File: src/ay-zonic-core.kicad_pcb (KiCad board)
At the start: 2 copper layers, 63.5 x 80.1 mm, 31 parts, among them SW1 ZON-X, U1 AY-3-8912, U2 74HCT74, U3 74HCT08, U4 74HCT11, U5 74HCT02

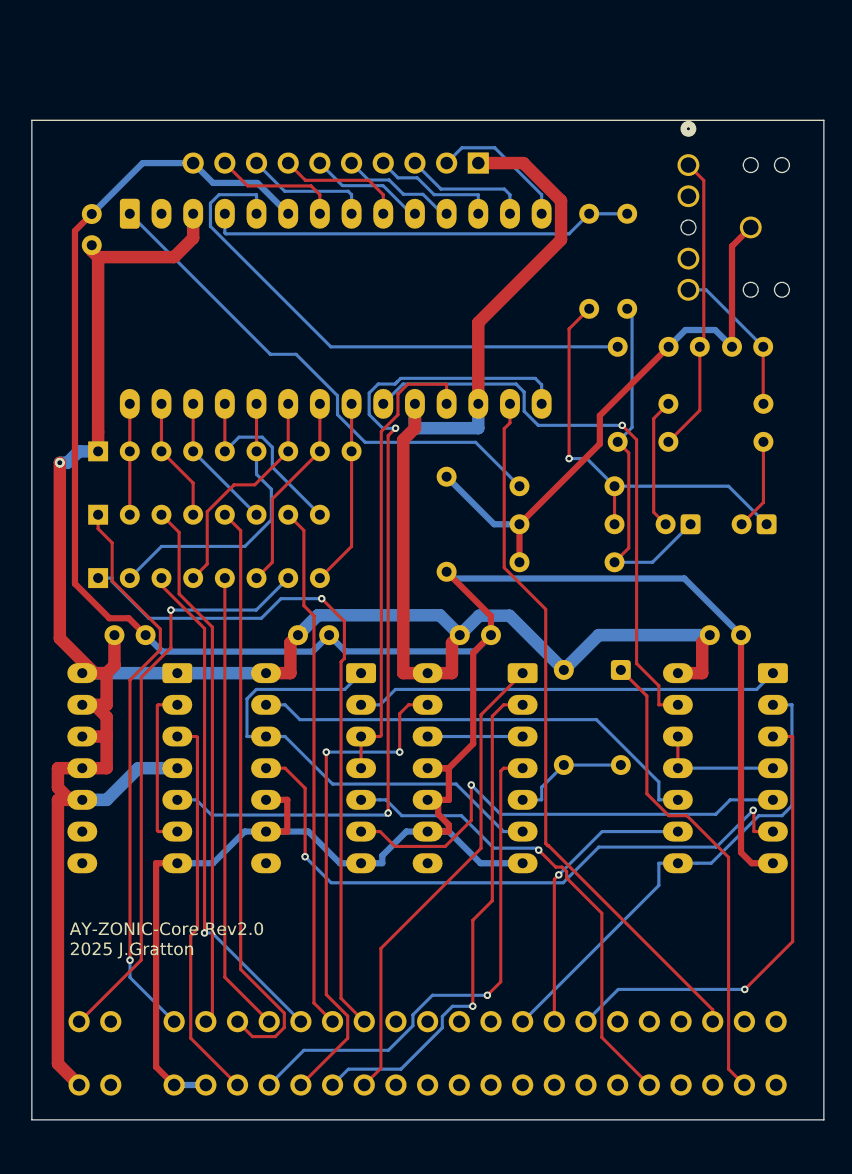
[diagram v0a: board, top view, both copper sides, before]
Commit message: added mounting holes and started routing.
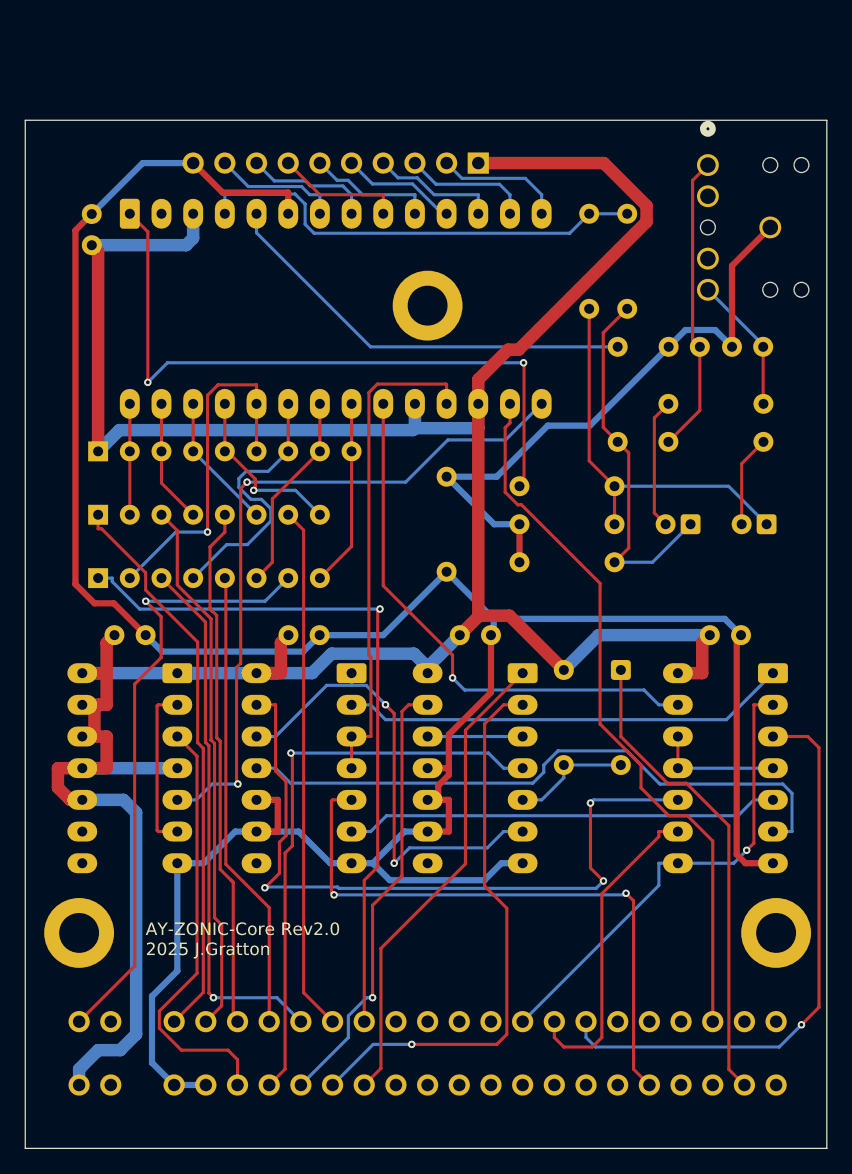
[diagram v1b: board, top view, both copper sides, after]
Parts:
- added H1: MountingHole, MountingHole:MountingHole_3.2mm_M3_DIN965_Pad, F.Cu at (123.2, 113.8)
- added H2: MountingHole, MountingHole:MountingHole_3.2mm_M3_DIN965_Pad, F.Cu at (67.3, 113.8)
- added H3: MountingHole, MountingHole:MountingHole_3.2mm_M3_DIN965_Pad, F.Cu at (95.2, 63.5)
- SW1: value ZON-X -> ZON X
- moved Line Out 1.56 mm to (117.7, 52.2)
- moved C7 0.76 mm to (84.1, 89.9)
- moved U3 0.76 mm to (89.2, 93.0)
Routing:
- net /IORD: track 37.0 -> 58.5 mm, vias 0 -> 3
- net /OUTC: track 41.2 -> 55.0 mm, vias 0 -> 2
- net /PSGCLK: track 69.2 -> 56.2 mm
- net VCC: track 234.9 -> 246.2 mm, vias 1 -> 0
- net /A7: track 38.7 -> 48.9 mm, vias 1 -> 2
- net /OUTA: track 44.0 -> 34.3 mm
- net /~{WR}: track 37.2 -> 46.5 mm
- net Net-(RN1-R5): track 23.1 -> 28.3 mm, vias 0 -> 1
- net /A0: track 41.3 -> 46.5 mm
- net /D2: track 47.6 -> 42.6 mm
- net GND: track 224.3 -> 219.7 mm
- net /A1: track 40.5 -> 35.9 mm, vias 2 -> 1
- net /BC1: track 47.2 -> 43.2 mm
- net /A2: track 41.1 -> 45.0 mm
- net Net-(U3-Pad6): track 38.7 -> 34.8 mm, vias 1 -> 0
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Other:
- board size 63.5 x 80.1 mm -> 64.3 x 82.4 mm

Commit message: updated routing
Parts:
- moved R4 1.52 mm to (112.8, 63.8)
- moved R5 1.52 mm to (109.7, 63.8)
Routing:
- net VCC: track 246.2 -> 220.6 mm
- net GND: track 219.7 -> 212.8 mm
- net /OUTA: track 34.3 -> 38.9 mm
- net /OUTC: track 55.0 -> 52.2 mm, vias 2 -> 1
- net /OUTB: track 36.7 -> 39.2 mm
- net Net-(RN1-R6): track 21.8 -> 23.9 mm
- net /IORD: track 58.5 -> 56.9 mm
- net Net-(RN1-R5): track 28.3 -> 29.9 mm
- net Net-(C2-Pad1): track 29.8 -> 31.0 mm
- net /~{IOREQ}: track 38.1 -> 36.9 mm
- net /LEFT: track 11.0 -> 12.1 mm
- net Net-(U2A-D): track 13.3 -> 12.4 mm
- net GND_AUDIO: track 49.6 -> 50.5 mm
- net /~{RESET}: track 57.6 -> 58.4 mm
- net Net-(C1-Pad1): track 31.6 -> 32.2 mm
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
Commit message: final route rev 2.0
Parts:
- added H4: MountingHole, MountingHole:MountingHole_3.2mm_M3_DIN965_Pad, F.Cu at (123.2, 45.7)
- SW1: value ZON X -> ZON-X
- moved H3 33.3 mm to (67.1, 45.7)
- moved I/O 5.59 mm to (99.3, 46.5)
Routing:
- net GND: track 212.8 -> 219.8 mm
- net /A2: track 45.0 -> 49.0 mm, vias 1 -> 0
- net /IOA5: track 9.90 -> 13.8 mm
- net /IOA3: track 9.30 -> 12.8 mm
- net /IOA7: track 9.72 -> 12.8 mm
- net /IOA4: track 9.75 -> 12.8 mm
- net /IOA2: track 10.2 -> 12.8 mm
- net /IOA6: track 10.2 -> 12.8 mm
- net /IOA0: track 10.2 -> 12.8 mm
- net /IOA1: track 10.2 -> 12.8 mm
- net VCC: track 220.6 -> 222.9 mm
- net /~{WR}: track 46.5 -> 46.3 mm, vias 1 -> 0
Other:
- board size 64.3 x 82.4 mm -> 64.3 x 90 mm

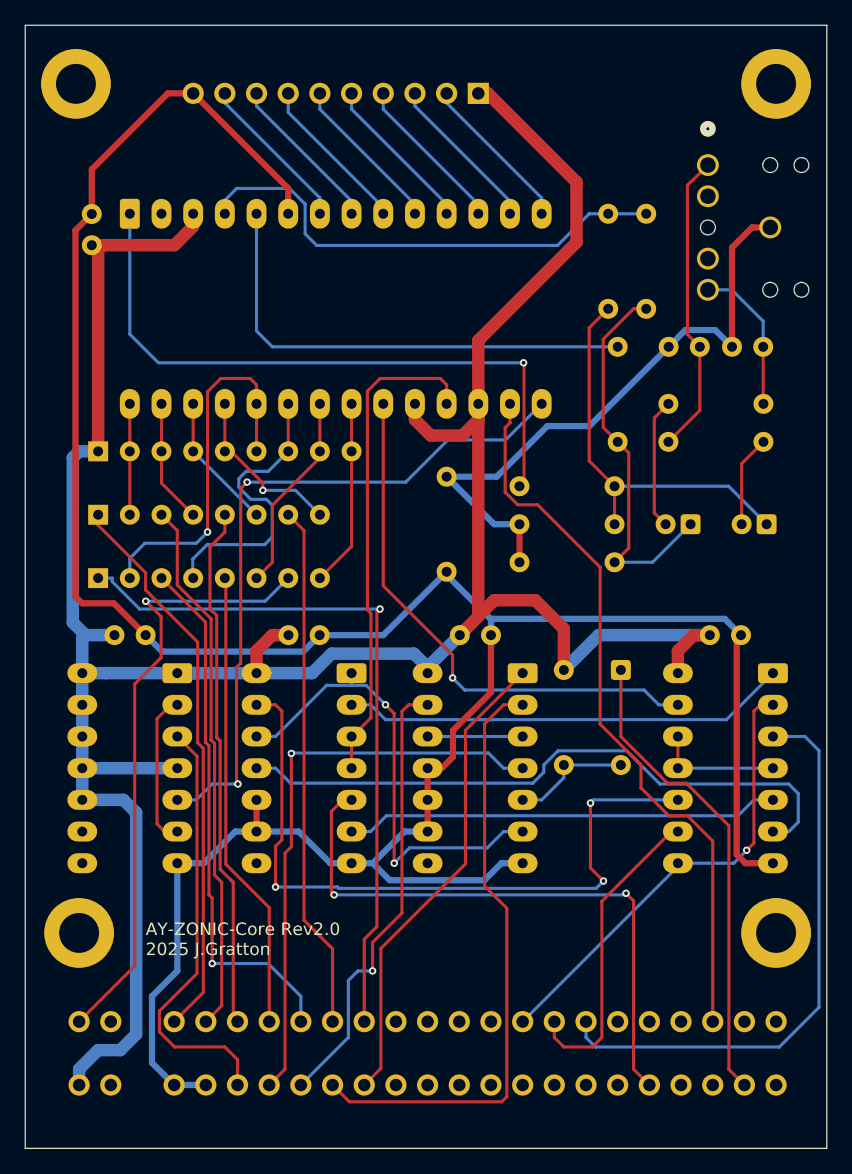
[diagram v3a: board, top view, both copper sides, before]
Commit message: rerouted a few things to make them better
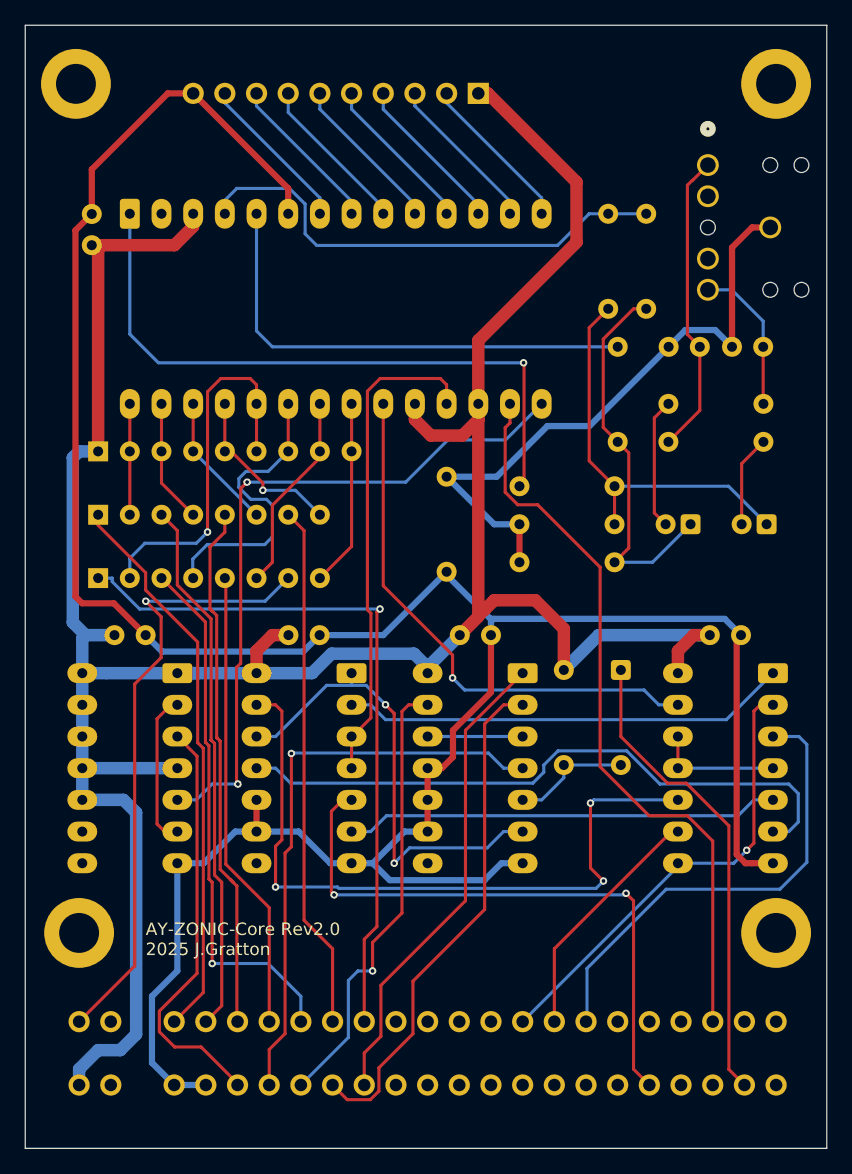
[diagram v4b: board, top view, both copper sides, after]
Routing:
- net /~{WR}: track 46.3 -> 37.9 mm
- net /A2: track 49.0 -> 41.1 mm
- net /~{RD}: track 25.0 -> 19.6 mm
- net /CLK: track 34.8 -> 33.7 mm
- net /~{RESET}: track 58.4 -> 59.3 mm
